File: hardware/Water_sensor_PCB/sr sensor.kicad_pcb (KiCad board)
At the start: 2 copper layers, 22 x 22 mm, 12 parts, among them J1 Conn_01x07_Pin, Q1 BPW40, Q2 BPW40, SW1 SW_Nidec_CAS-120A1

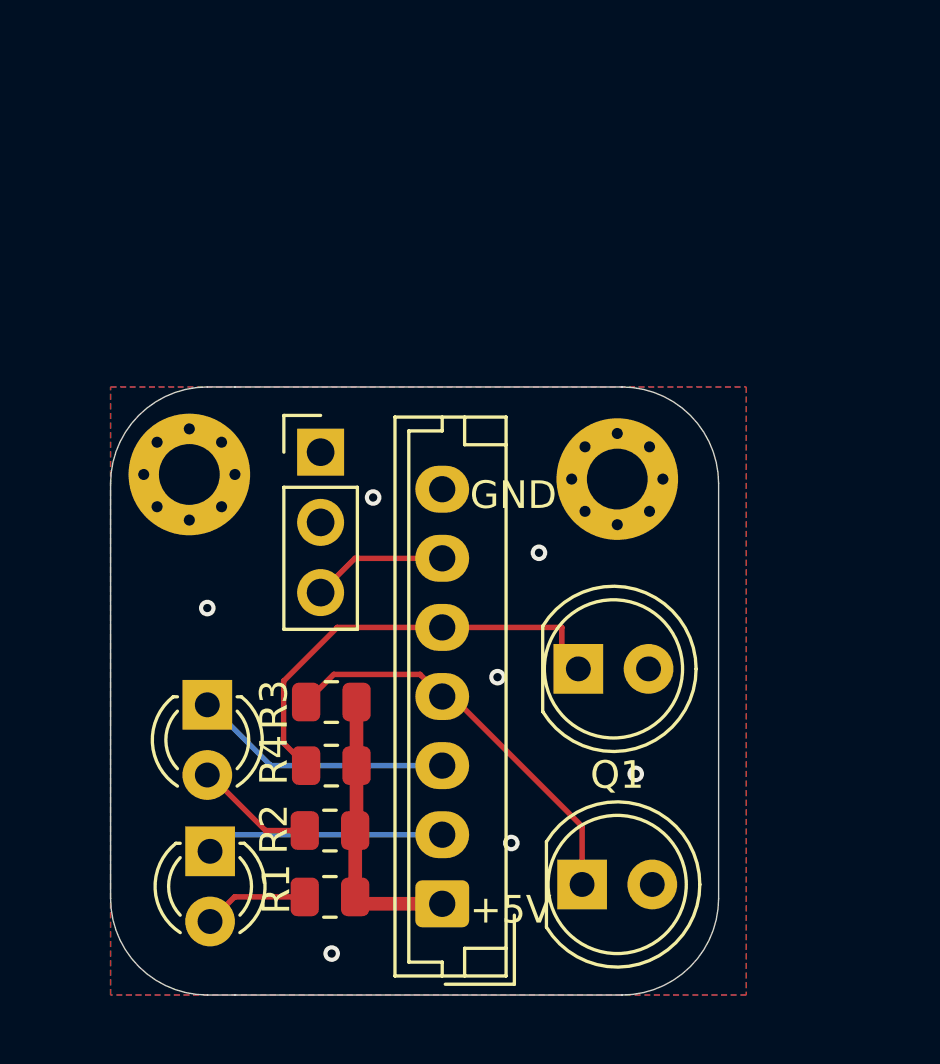
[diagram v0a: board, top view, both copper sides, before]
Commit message: changed JST connector size, changed silkscreen
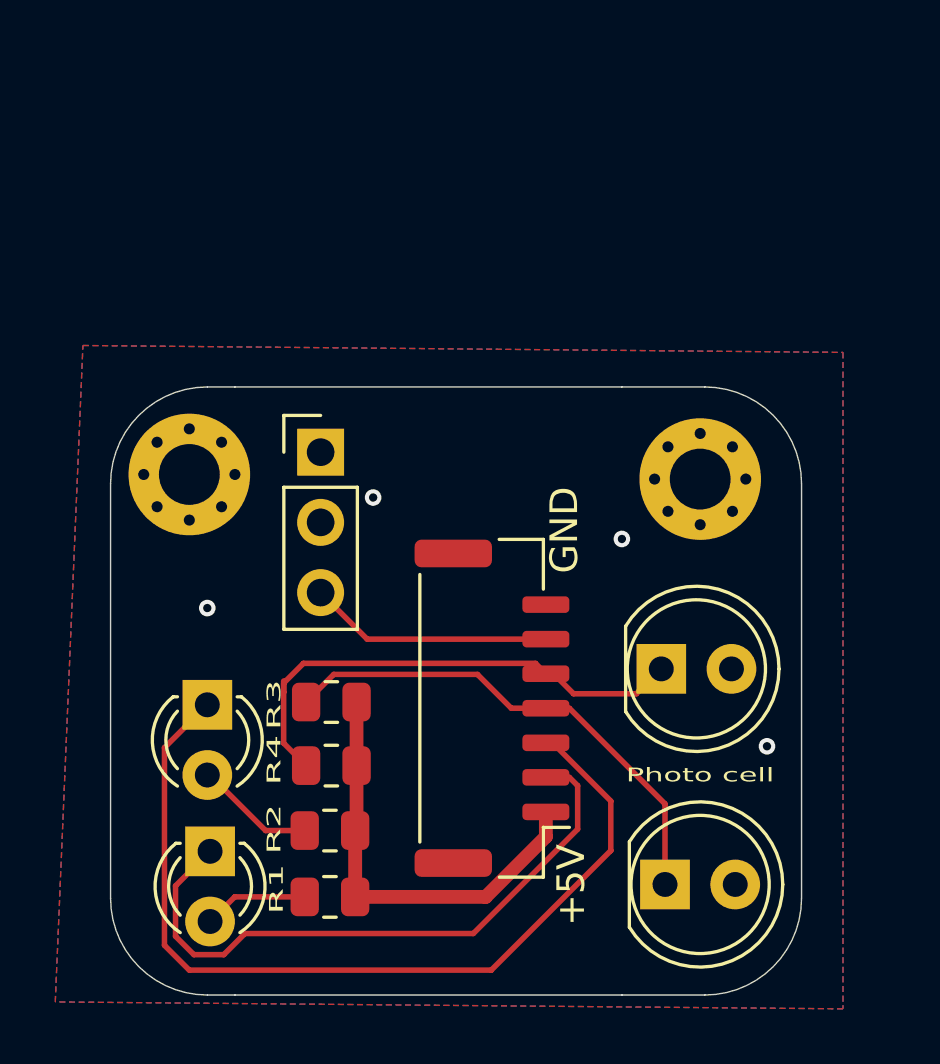
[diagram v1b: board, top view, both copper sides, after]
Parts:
- J1: footprint Connector_JST:JST_EH_B7B-EH-A_1x07_P2.50mm_Vertical -> Connector_JST:JST_GH_BM07B-GHS-TBT_1x07-1MP_P1.25mm_Vertical
- Photo cell: renamed from Q1
- moved J1 7.30 mm to (109.8, 83.1)
- moved H2 3.00 mm to (117.3, 74.8)
- moved Photo cell 3.00 mm to (116.1, 89.5)
- moved Q2 3.00 mm to (115.9, 81.7)
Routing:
- net DRAIN2: track 9.31 -> 32.7 mm
- net DRAIN1: track 8.65 -> 24.0 mm
- net +5V: track 10.3 -> 16.1 mm
- net SWITCH: track 4.91 -> 8.85 mm
- net CH0: track 14.8 -> 18.3 mm
- net CH1: track 16.0 -> 19.4 mm
- net GND: vias 7 -> 4
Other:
- board size 22 x 22 mm -> 25 x 22 mm

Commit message: feat: Cleanup and redesign of sensor pcb
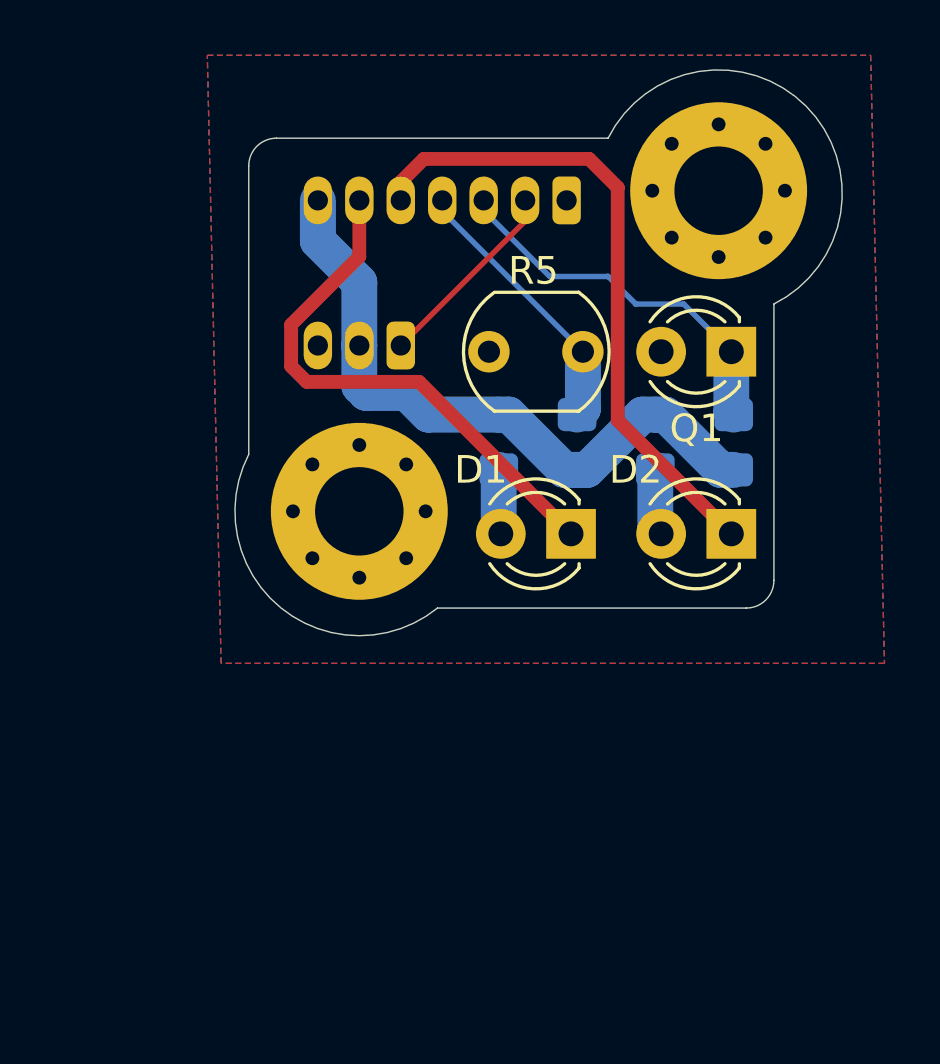
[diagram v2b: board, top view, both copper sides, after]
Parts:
- removed Photo cell: BPW40, LED_THT:LED_D5.0mm_Clear
- removed Q2: BPW40, LED_THT:LED_D5.0mm_Clear
- added Q1: LTR-4206E, LED_THT:LED_D3.0mm, F.Cu at (118.5, 70.2)
- added R5: PDV-P8101, OptoDevice:R_LDR_5.1x4.3mm_P3.4mm_Vertical, F.Cu at (113.1, 70.2)
- D1: value LED -> WHITE
- H1, H2: footprint MountingHole:MountingHole_2.2mm_M2_Pad_Via -> MountingHole:MountingHole_3.2mm_M3_Pad_Via
- J1: footprint Connector_JST:JST_GH_BM07B-GHS-TBT_1x07-1MP_P1.25mm_Vertical -> Connector_JST:JST_ZH_B7B-ZR_1x07_P1.50mm_Vertical; moved to B.Cu
- R1, R3: footprint Resistor_SMD:R_0805_2012Metric -> Resistor_SMD:R_0805_2012Metric_Pad1.20x1.40mm_HandSolder; moved to B.Cu
- R2: value R -> 39; footprint Resistor_SMD:R_0805_2012Metric -> Resistor_SMD:R_0805_2012Metric_Pad1.20x1.40mm_HandSolder; moved to B.Cu
- R4: value R -> 560; footprint Resistor_SMD:R_0805_2012Metric -> Resistor_SMD:R_0805_2012Metric_Pad1.20x1.40mm_HandSolder; moved to B.Cu
- SW1: footprint Connector_PinHeader_2.54mm:PinHeader_1x03_P2.54mm_Vertical -> Connector_JST:JST_ZH_B3B-ZR_1x03_P1.50mm_Vertical; moved to B.Cu
- moved D2 19.9 mm to (118.5, 76.8), turned to 180 degrees
- moved R4 18.7 mm to (118.5, 73.5), turned to -90 degrees
- moved J1 18.6 mm to (112.5, 64.8), turned to 180 degrees
- moved R2 18.3 mm to (115.7, 73.5), turned to 90 degrees
- moved R1 17.5 mm to (110.0, 73.5), turned to 90 degrees
- moved D1 17.4 mm to (112.7, 76.8), turned to 180 degrees
- moved R3 12.9 mm to (112.9, 73.5), turned to -90 degrees
- moved H2 10.5 mm to (118.0, 64.4)
- moved H1 6.29 mm to (105.0, 76.0)
- moved SW1 4.83 mm to (106.5, 70.0), turned to 180 degrees
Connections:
- J1 pad 1: +5V -> GND
- J1 pad 2: DRAIN1 -> SWITCH
- J1 pad 3: DRAIN2 -> CH1
- J1 pad 5: CH1 -> DRAIN2
- J1 pad 6: SWITCH -> DRAIN1
- J1 pad 7: GND -> +5V
- SW1 pad 1: unconnected-(SW1-C-Pad1) -> SWITCH
- SW1 pad 2: GND -> +5V
- SW1 pad 3: SWITCH -> unconnected-(SW1-A-Pad3)
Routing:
- net DRAIN2: track 32.7 -> 23.5 mm
- net CH0: track 18.3 -> 9.95 mm
- net +5V: track 16.1 -> 23.8 mm
- net CH1: track 19.4 -> 13.8 mm
- net DRAIN1: track 24.0 -> 19.7 mm
- net Net-(D2-A): track 4.26 -> 2.40 mm
- net SWITCH: track 8.85 -> 7.11 mm
- net Net-(D1-A): track 3.79 -> 2.35 mm
- net GND: vias 4 -> 0
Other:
- board size 25 x 22 mm -> 22 x 20.5 mm
- board text removed: "+5V"
- board text removed: "GND"
